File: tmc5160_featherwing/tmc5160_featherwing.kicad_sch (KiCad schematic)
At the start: 3 parts, among them U1 TMC5160A-TA, U2 BUK7D36-60EX, U3 BUK7D36-60EX

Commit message: Add sheets
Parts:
- removed U1: TMC5160A-TA, Package_QFP:TQFP-48-1EP_7x7mm_P0.5mm_EP5x5mm_ThermalVias, symbol Driver_Motor:TMC5160A-TA
- removed U2, U3: BUK7D36-60EX, Janelia:BUK7D3660EX_NEX, symbol Janelia:BUK7D36-60EX
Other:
- added sheet assembly (assembly.kicad_sch)
- added sheet driver_controller (driver_controller.kicad_sch)
- added sheet power (power.kicad_sch)
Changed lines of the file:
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@@
   (title_block
     (title "tmc5160_featherwing")
-    (date "2024-03-21")
+    (date "2024-03-22")
     (rev "1.0")
     (company "Howard Hughes Medical Institute")
   )
-  (symbol (lib_id "Driver_Motor:TMC5160A-TA") (at 49.53 109.22 0) (unit 1)
-    (in_bom yes) (on_board yes) (dnp no) (fields_autoplaced)
-    (property "Reference" "U1" (at 54.2641 147.32 0)
-      (effects (font (size 1.27 1.27)) (justify left))
+  (wire (pts (xy 57.15 38.1) (xy 59.69 38.1))
+    (stroke (width 0) (type default))
+  )
+  (label "GND" (at 57.15 38.1 180) (fields_autoplaced)
+    (effects (font (size 1.27 1.27)) (justify right bottom))
+  )
+  (sheet (at 59.69 60.96) (size 13.97 3.81) (fields_autoplaced)
+    (stroke (width 0.1524) (type solid))
+    (fill (color 0 0 0 0.0000))
+    (property "Sheetname" "driver_controller" (at 59.69 60.2484 0)
+      (effects (font (size 1.27 1.27)) (justify left bottom))
     )
-    (property "Value" "TMC5160A-TA" (at 54.2641 149.86 0)
-      (effects (font (size 1.27 1.27)) (justify left))
+    (property "Sheetfile" "driver_controller.kicad_sch" (at 59.69 65.3546 0)
+      (effects (font (size 1.27 1.27)) (justify left top))
     )
-    (property "Footprint" "Package_QFP:TQFP-48-1EP_7x7mm_P0.5mm_EP5x5mm_ThermalVias" (at 49.53 160.02 0)
-      (effects (font (size 1.27 1.27)) hide)
-    )
-    (property "Datasheet" "https://www.trinamic.com/fileadmin/assets/Products/ICs_Documents/TMC5160A_Datasheet_Rev1.14.pdf" (at 49.53 99.06 0)
-      (effects (font (size 1.27 1.27)) hide)
-    )
-    (pin "20")
-    (pin "3")
-    (pin "37")
-    (pin "38")
-    (pin "8")
-    (pin "47")
-    (pin "49")
-    (pin "21")
-    (pin "33")
-    (pin "35")
-    (pin "9")
-    (pin "5")
-    (pin "14")
-    (pin "11")
-    (pin "15")
-    (pin "6")
-    (pin "18")
-    (pin "41")
-    (pin "43")
-    (pin "32")
-    (pin "26")
-    (pin "48")
-    (pin "39")
-    (pin "17")
-    (pin "7")
-    (pin "30")
-    (pin "29")
-    (pin "34")
-    (pin "46")
-    (pin "24")
-    (pin "31")
-    (pin "25")
-    (pin "19")
-    (pin "2")
-    (pin "4")
-    (pin "28")
-    (pin "16")
-    (pin "23")
-    (pin "36")
-    (pin "10")
-    (pin "40")
-    (pin "22")
-    (pin "27")
-    (pin "44")
-    (pin "13")
-    (pin "12")
-    (pin "1")
-    (pin "45")
-    (pin "42")
     (instances
       (project "tmc5160_featherwing"
-        (path "/df2b2e89-e055-4140-95de-f1df723db034"
-          (reference "U1") (unit 1)
-        )
+        (path "/df2b2e89-e055-4140-95de-f1df723db034" (page "4"))
       )
     )
   )
-  (symbol (lib_id "Janelia:BUK7D36-60EX") (at 180.34 53.34 0) (unit 1)
-    (in_bom yes) (on_board yes) (dnp no) (fields_autoplaced)
-    (property "Reference" "U3" (at 172.72 60.96 0) (do_not_autoplace)
-      (effects (font (size 1.524 1.524)))
+  (sheet (at 59.69 35.56) (size 12.7 5.08) (fields_autoplaced)
+    (stroke (width 0.1524) (type solid))
+    (fill (color 0 0 0 0.0000))
+    (property "Sheetname" "assembly" (at 59.69 34.8484 0)
+      (effects (font (size 1.27 1.27)) (justify left bottom))
     )
-    (property "Value" "BUK7D36-60EX" (at 189.23 53.34 90) (do_not_autoplace)
-      (effects (font (size 1.524 1.524)))
+    (property "Sheetfile" "assembly.kicad_sch" (at 59.69 41.2246 0)
+      (effects (font (size 1.27 1.27)) (justify left top))
     )
-    (property "Footprint" "Janelia:BUK7D3660EX_NEX" (at 180.34 22.86 0)
-      (effects (font (size 1.27 1.27) italic) hide)
+    (pin "GND" passive (at 59.69 38.1 180)
+      (effects (font (size 1.27 1.27)) (justify left))
     )
-    (property "Datasheet" "BUK7D36-60EX" (at 180.34 27.94 0)
-      (effects (font (size 1.27 1.27) italic) hide)
-    )
-    (property "Description" "MOSFET N-CH 60V 5.5A/14A" (at 180.34 30.48 0)
-      (effects (font (size 1.27 1.27)) hide)
-    )
-    (property "Package" "6DFN" (at 180.34 15.24 0)
-      (effects (font (size 1.27 1.27)) hide)
-    )
-    (property "Manufacturer" "Nexperia USA Inc." (at 180.34 20.32 0)
-      (effects (font (size 1.27 1.27)) hide)
-    )
-    (property "Manufacturer Part Number" "BUK7D36-60EX" (at 180.34 12.7 0)
-      (effects (font (size 1.27 1.27)) hide)
-    )
-    (property "Vendor" "Digi-Key" (at 180.34 17.78 0)
-      (effects (font (size 1.27 1.27)) hide)
-    )
-    (property "Vendor Part Number" "1727-BUK7D36-60EXCT-ND" (at 180.34 25.4 0)
-      (effects (font (size 1.27 1.27)) hide)
-    )
-    (pin "4")
-    (pin "5")
-    (pin "6")
-    (pin "8")
-    (pin "3")
-    (pin "2")
-    (pin "1")
-    (pin "7")
     (instances
       (project "tmc5160_featherwing"
-        (path "/df2b2e89-e055-4140-95de-f1df723db034"
-          (reference "U3") (unit 1)
-        )
+        (path "/df2b2e89-e055-4140-95de-f1df723db034" (page "2"))
       )
     )
   )
-  (symbol (lib_id "Janelia:BUK7D36-60EX") (at 135.89 53.34 0) (unit 1)
-    (in_bom yes) (on_board yes) (dnp no) (fields_autoplaced)
-    (property "Reference" "U2" (at 128.27 60.96 0) (do_not_autoplace)
-      (effects (font (size 1.524 1.524)))
+  (sheet (at 59.69 49.53) (size 12.7 3.81) (fields_autoplaced)
+    (stroke (width 0.1524) (type solid))
+    (fill (color 0 0 0 0.0000))
+    (property "Sheetname" "power" (at 59.69 48.8184 0)
+      (effects (font (size 1.27 1.27)) (justify left bottom))
     )
-    (property "Value" "BUK7D36-60EX" (at 144.78 53.34 90) (do_not_autoplace)
-      (effects (font (size 1.524 1.524)))
+    (property "Sheetfile" "power.kicad_sch" (at 59.69 53.9246 0)
+      (effects (font (size 1.27 1.27)) (justify left top))
     )
-    (property "Footprint" "Janelia:BUK7D3660EX_NEX" (at 135.89 22.86 0)
-      (effects (font (size 1.27 1.27) italic) hide)
-    )
-    (property "Datasheet" "BUK7D36-60EX" (at 135.89 27.94 0)
-      (effects (font (size 1.27 1.27) italic) hide)
-    )
-    (property "Description" "MOSFET N-CH 60V 5.5A/14A" (at 135.89 30.48 0)
-      (effects (font (size 1.27 1.27)) hide)
-    )
-    (property "Package" "6DFN" (at 135.89 15.24 0)
-      (effects (font (size 1.27 1.27)) hide)
-    )
-    (property "Manufacturer" "Nexperia USA Inc." (at 135.89 20.32 0)
-      (effects (font (size 1.27 1.27)) hide)
-    )
-    (property "Manufacturer Part Number" "BUK7D36-60EX" (at 135.89 12.7 0)
-      (effects (font (size 1.27 1.27)) hide)
-    )
-    (property "Vendor" "Digi-Key" (at 135.89 17.78 0)
-      (effects (font (size 1.27 1.27)) hide)
-    )
-    (property "Vendor Part Number" "1727-BUK7D36-60EXCT-ND" (at 135.89 25.4 0)
-      (effects (font (size 1.27 1.27)) hide)
-    )
-    (pin "2")
-    (pin "7")
-    (pin "6")
-    (pin "5")
-    (pin "4")
-    (pin "3")
-    (pin "1")
-    (pin "8")
     (instances
       (project "tmc5160_featherwing"
-        (path "/df2b2e89-e055-4140-95de-f1df723db034"
-          (reference "U2") (unit 1)
-        )
+        (path "/df2b2e89-e055-4140-95de-f1df723db034" (page "3"))
       )
     )

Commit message: Add connectors
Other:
- added sheet featherwing (featherwing.kicad_sch)
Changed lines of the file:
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@@
   (title_block
     (title "tmc5160_featherwing")
-    (date "2024-03-22")
+    (date "2024-03-25")
     (rev "1.0")
     (company "Howard Hughes Medical Institute")
@@
     (effects (font (size 1.27 1.27)) (justify right bottom))
   )
-  (sheet (at 59.69 60.96) (size 13.97 3.81) (fields_autoplaced)
+  (sheet (at 59.69 72.39) (size 13.97 3.81) (fields_autoplaced)
     (stroke (width 0.1524) (type solid))
     (fill (color 0 0 0 0.0000))
-    (property "Sheetname" "driver_controller" (at 59.69 60.2484 0)
+    (property "Sheetname" "driver_controller" (at 59.69 71.6784 0)
       (effects (font (size 1.27 1.27)) (justify left bottom))
     )
-    (property "Sheetfile" "driver_controller.kicad_sch" (at 59.69 65.3546 0)
+    (property "Sheetfile" "driver_controller.kicad_sch" (at 59.69 76.7846 0)
       (effects (font (size 1.27 1.27)) (justify left top))
     )
@@
     )
   )
-  (sheet (at 59.69 49.53) (size 12.7 3.81) (fields_autoplaced)
+  (sheet (at 59.69 48.26) (size 12.7 3.81) (fields_autoplaced)
     (stroke (width 0.1524) (type solid))
     (fill (color 0 0 0 0.0000))
-    (property "Sheetname" "power" (at 59.69 48.8184 0)
+    (property "Sheetname" "featherwing" (at 59.69 47.5484 0)
       (effects (font (size 1.27 1.27)) (justify left bottom))
     )
-    (property "Sheetfile" "power.kicad_sch" (at 59.69 53.9246 0)
+    (property "Sheetfile" "featherwing.kicad_sch" (at 59.69 52.6546 0)
       (effects (font (size 1.27 1.27)) (justify left top))
     )
+    (instances
+      (project "tmc5160_featherwing"
+        (path "/df2b2e89-e055-4140-95de-f1df723db034" (page "13"))
+      )
+    )
+  )
+  (sheet (at 59.69 60.96) (size 12.7 3.81) (fields_autoplaced)
+    (stroke (width 0.1524) (type solid))
+    (fill (color 0 0 0 0.0000))
+    (property "Sheetname" "power" (at 59.69 60.2484 0)
+      (effects (font (size 1.27 1.27)) (justify left bottom))
+    )
+    (property "Sheetfile" "power.kicad_sch" (at 59.69 65.3546 0)
+      (effects (font (size 1.27 1.27)) (justify left top))
+    )

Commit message: Add to power sheet
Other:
- sheet power ports: added ENABLE, GND, VIO, VM; removed none
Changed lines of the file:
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@@
   (title_block
     (title "tmc5160_featherwing")
-    (date "2024-04-04")
+    (date "2024-04-05")
     (rev "1.0")
     (company "Howard Hughes Medical Institute")
   )
-  (wire (pts (xy 57.15 38.1) (xy 59.69 38.1))
+  (wire (pts (xy 77.47 48.26) (xy 74.93 48.26))
     (stroke (width 0) (type default))
   )
-  (label "GND" (at 57.15 38.1 180) (fields_autoplaced)
+  (wire (pts (xy 55.88 38.1) (xy 58.42 38.1))
+    (stroke (width 0) (type default))
+  )
+  (wire (pts (xy 77.47 53.34) (xy 74.93 53.34))
+    (stroke (width 0) (type default))
+  )
+  (wire (pts (xy 77.47 50.8) (xy 74.93 50.8))
+    (stroke (width 0) (type default))
+  )
+  (label "GND" (at 77.47 53.34 0) (fields_autoplaced)
+    (effects (font (size 1.27 1.27)) (justify left bottom))
+  )
+  (label "VIO" (at 77.47 50.8 0) (fields_autoplaced)
+    (effects (font (size 1.27 1.27)) (justify left bottom))
+  )
+  (label "GND" (at 55.88 38.1 180) (fields_autoplaced)
     (effects (font (size 1.27 1.27)) (justify right bottom))
   )
-  (sheet (at 59.69 72.39) (size 13.97 3.81) (fields_autoplaced)
+  (label "VM" (at 77.47 48.26 0) (fields_autoplaced)
+    (effects (font (size 1.27 1.27)) (justify left bottom))
+  )
+  (sheet (at 58.42 78.74) (size 13.97 3.81) (fields_autoplaced)
     (stroke (width 0.1524) (type solid))
     (fill (color 0 0 0 0.0000))
-    (property "Sheetname" "driver_controller" (at 59.69 71.6784 0)
+    (property "Sheetname" "driver_controller" (at 58.42 78.0284 0)
       (effects (font (size 1.27 1.27)) (justify left bottom))
     )
-    (property "Sheetfile" "driver_controller.kicad_sch" (at 59.69 76.7846 0)
+    (property "Sheetfile" "driver_controller.kicad_sch" (at 58.42 83.1346 0)
       (effects (font (size 1.27 1.27)) (justify left top))
     )
@@
     )
   )
-  (sheet (at 59.69 35.56) (size 12.7 5.08) (fields_autoplaced)
+  (sheet (at 58.42 35.56) (size 12.7 5.08) (fields_autoplaced)
     (stroke (width 0.1524) (type solid))
     (fill (color 0 0 0 0.0000))
-    (property "Sheetname" "assembly" (at 59.69 34.8484 0)
+    (property "Sheetname" "assembly" (at 58.42 34.8484 0)
       (effects (font (size 1.27 1.27)) (justify left bottom))
     )
-    (property "Sheetfile" "assembly.kicad_sch" (at 59.69 41.2246 0)
+    (property "Sheetfile" "assembly.kicad_sch" (at 58.42 41.2246 0)
       (effects (font (size 1.27 1.27)) (justify left top))
     )
-    (pin "GND" passive (at 59.69 38.1 180)
+    (pin "GND" passive (at 58.42 38.1 180)
       (effects (font (size 1.27 1.27)) (justify left))
     )
@@
     )
   )
-  (sheet (at 59.69 48.26) (size 12.7 3.81) (fields_autoplaced)
+  (sheet (at 58.42 63.5) (size 12.7 3.81) (fields_autoplaced)
     (stroke (width 0.1524) (type solid))
     (fill (color 0 0 0 0.0000))
-    (property "Sheetname" "featherwing" (at 59.69 47.5484 0)
+    (property "Sheetname" "featherwing" (at 58.42 62.7884 0)
       (effects (font (size 1.27 1.27)) (justify left bottom))
     )
-    (property "Sheetfile" "featherwing.kicad_sch" (at 59.69 52.6546 0)
+    (property "Sheetfile" "featherwing.kicad_sch" (at 58.42 67.8946 0)
       (effects (font (size 1.27 1.27)) (justify left top))
     )
@@
     )
   )
-  (sheet (at 59.69 60.96) (size 12.7 3.81) (fields_autoplaced)
+  (sheet (at 58.42 45.72) (size 16.51 10.16) (fields_autoplaced)
     (stroke (width 0.1524) (type solid))
     (fill (color 0 0 0 0.0000))
-    (property "Sheetname" "power" (at 59.69 60.2484 0)
+    (property "Sheetname" "power" (at 58.42 45.0084 0)
       (effects (font (size 1.27 1.27)) (justify left bottom))
     )
-    (property "Sheetfile" "power.kicad_sch" (at 59.69 65.3546 0)
+    (property "Sheetfile" "power.kicad_sch" (at 58.42 56.4646 0)
       (effects (font (size 1.27 1.27)) (justify left top))
     )
+    (pin "GND" passive (at 74.93 53.34 0)
+      (effects (font (size 1.27 1.27)) (justify right))
+    )
+    (pin "VM" passive (at 74.93 48.26 0)
+      (effects (font (size 1.27 1.27)) (justify right))
+    )
+    (pin "VIO" passive (at 74.93 50.8 0)
+      (effects (font (size 1.27 1.27)) (justify right))
+    )
+    (pin "ENABLE" input (at 58.42 50.8 180)
+      (effects (font (size 1.27 1.27)) (justify left))
+    )
     (instances

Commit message: Add parts
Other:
- sheet driver_controller ports: added GND, VIO, VM; removed none
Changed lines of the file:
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@@
   (title_block
     (title "tmc5160_featherwing")
-    (date "2024-04-05")
+    (date "2024-04-10")
     (rev "1.0")
     (company "Howard Hughes Medical Institute")
+  )
+  (wire (pts (xy 55.88 83.82) (xy 58.42 83.82))
+    (stroke (width 0) (type default))
   )
   (wire (pts (xy 77.47 48.26) (xy 74.93 48.26))
@@
   )
   (wire (pts (xy 55.88 38.1) (xy 58.42 38.1))
+    (stroke (width 0) (type default))
+  )
+  (wire (pts (xy 55.88 81.28) (xy 58.42 81.28))
+    (stroke (width 0) (type default))
+  )
+  (wire (pts (xy 55.88 86.36) (xy 58.42 86.36))
     (stroke (width 0) (type default))
   )
@@
     (effects (font (size 1.27 1.27)) (justify left bottom))
   )
+  (label "VIO" (at 55.88 83.82 180) (fields_autoplaced)
+    (effects (font (size 1.27 1.27)) (justify right bottom))
+  )
+  (label "VM" (at 55.88 81.28 180) (fields_autoplaced)
+    (effects (font (size 1.27 1.27)) (justify right bottom))
+  )
   (label "GND" (at 55.88 38.1 180) (fields_autoplaced)
+    (effects (font (size 1.27 1.27)) (justify right bottom))
+  )
+  (label "GND" (at 55.88 86.36 180) (fields_autoplaced)
     (effects (font (size 1.27 1.27)) (justify right bottom))
   )
@@
     (effects (font (size 1.27 1.27)) (justify left bottom))
   )
-  (sheet (at 58.42 78.74) (size 13.97 3.81) (fields_autoplaced)
+  (sheet (at 58.42 78.74) (size 16.51 12.7) (fields_autoplaced)
     (stroke (width 0.1524) (type solid))
     (fill (color 0 0 0 0.0000))
@@
       (effects (font (size 1.27 1.27)) (justify left bottom))
     )
-    (property "Sheetfile" "driver_controller.kicad_sch" (at 58.42 83.1346 0)
+    (property "Sheetfile" "driver_controller.kicad_sch" (at 58.42 92.0246 0)
       (effects (font (size 1.27 1.27)) (justify left top))
     )
+    (pin "VM" passive (at 58.42 81.28 180)
+      (effects (font (size 1.27 1.27)) (justify left))
+    )
+    (pin "VIO" passive (at 58.42 83.82 180)
+      (effects (font (size 1.27 1.27)) (justify left))
+    )
+    (pin "GND" passive (at 58.42 86.36 180)
+      (effects (font (size 1.27 1.27)) (justify left))
+    )
     (instances

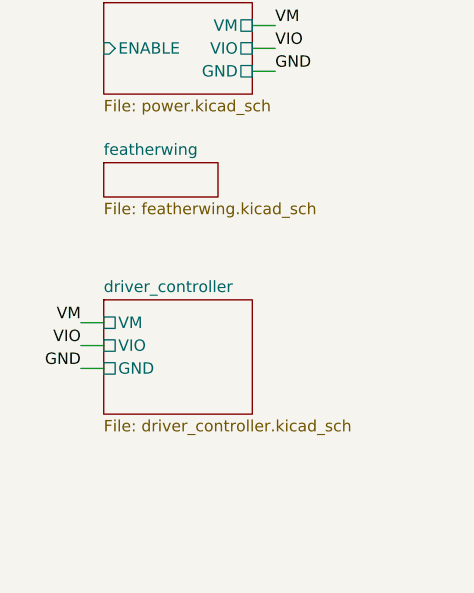
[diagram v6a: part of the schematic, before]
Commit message: Add capacitors and resistors
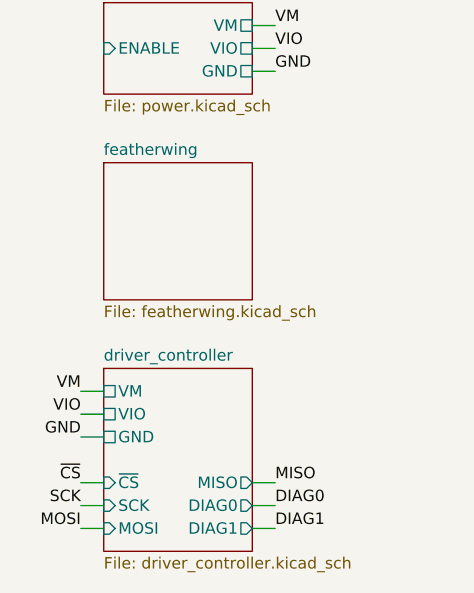
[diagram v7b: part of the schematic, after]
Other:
- sheet driver_controller ports: added DIAG0, DIAG1, MISO, MOSI, SCK, ~{CS}; removed none
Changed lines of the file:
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@@
   (title_block
     (title "tmc5160_featherwing")
-    (date "2024-04-11")
+    (date "2024-04-12")
     (rev "1.0")
     (company "Howard Hughes Medical Institute")
   )
-  (wire (pts (xy 55.88 83.82) (xy 58.42 83.82))
+  (wire (pts (xy 58.42 101.6) (xy 55.88 101.6))
+    (stroke (width 0) (type default))
+  )
+  (wire (pts (xy 55.88 91.44) (xy 58.42 91.44))
+    (stroke (width 0) (type default))
+  )
+  (wire (pts (xy 58.42 104.14) (xy 55.88 104.14))
     (stroke (width 0) (type default))
   )
@@
     (stroke (width 0) (type default))
   )
+  (wire (pts (xy 58.42 99.06) (xy 55.88 99.06))
+    (stroke (width 0) (type default))
+  )
+  (wire (pts (xy 74.93 104.14) (xy 77.47 104.14))
+    (stroke (width 0) (type default))
+  )
   (wire (pts (xy 55.88 38.1) (xy 58.42 38.1))
     (stroke (width 0) (type default))
   )
-  (wire (pts (xy 55.88 81.28) (xy 58.42 81.28))
+  (wire (pts (xy 55.88 88.9) (xy 58.42 88.9))
     (stroke (width 0) (type default))
   )
-  (wire (pts (xy 55.88 86.36) (xy 58.42 86.36))
+  (wire (pts (xy 74.93 101.6) (xy 77.47 101.6))
+    (stroke (width 0) (type default))
+  )
+  (wire (pts (xy 74.93 99.06) (xy 77.47 99.06))
+    (stroke (width 0) (type default))
+  )
+  (wire (pts (xy 55.88 93.98) (xy 58.42 93.98))
     (stroke (width 0) (type default))
   )
@@
     (effects (font (size 1.27 1.27)) (justify left bottom))
   )
+  (label "DIAG1" (at 77.47 104.14 0) (fields_autoplaced)
+    (effects (font (size 1.27 1.27)) (justify left bottom))
+  )
   (label "VIO" (at 77.47 50.8 0) (fields_autoplaced)
     (effects (font (size 1.27 1.27)) (justify left bottom))
   )
-  (label "VIO" (at 55.88 83.82 180) (fields_autoplaced)
+  (label "MOSI" (at 55.88 104.14 180) (fields_autoplaced)
     (effects (font (size 1.27 1.27)) (justify right bottom))
   )
-  (label "VM" (at 55.88 81.28 180) (fields_autoplaced)
+  (label "VIO" (at 55.88 91.44 180) (fields_autoplaced)
     (effects (font (size 1.27 1.27)) (justify right bottom))
+  )
+  (label "VM" (at 55.88 88.9 180) (fields_autoplaced)
+    (effects (font (size 1.27 1.27)) (justify right bottom))
+  )
+  (label "DIAG0" (at 77.47 101.6 0) (fields_autoplaced)
+    (effects (font (size 1.27 1.27)) (justify left bottom))
   )
   (label "GND" (at 55.88 38.1 180) (fields_autoplaced)
     (effects (font (size 1.27 1.27)) (justify right bottom))
   )
-  (label "GND" (at 55.88 86.36 180) (fields_autoplaced)
+  (label "GND" (at 55.88 93.98 180) (fields_autoplaced)
+    (effects (font (size 1.27 1.27)) (justify right bottom))
+  )
+  (label "MISO" (at 77.47 99.06 0) (fields_autoplaced)
+    (effects (font (size 1.27 1.27)) (justify left bottom))
+  )
+  (label "SCK" (at 55.88 101.6 180) (fields_autoplaced)
+    (effects (font (size 1.27 1.27)) (justify right bottom))
+  )
+  (label "~{CS}" (at 55.88 99.06 180) (fields_autoplaced)
     (effects (font (size 1.27 1.27)) (justify right bottom))
   )
@@
     (effects (font (size 1.27 1.27)) (justify left bottom))
   )
-  (sheet (at 58.42 78.74) (size 16.51 12.7) (fields_autoplaced)
+  (sheet (at 58.42 86.36) (size 16.51 20.32) (fields_autoplaced)
     (stroke (width 0.1524) (type solid))
     (fill (color 0 0 0 0.0000))
-    (property "Sheetname" "driver_controller" (at 58.42 78.0284 0)
+    (property "Sheetname" "driver_controller" (at 58.42 85.6484 0)
       (effects (font (size 1.27 1.27)) (justify left bottom))
     )
-    (property "Sheetfile" "driver_controller.kicad_sch" (at 58.42 92.0246 0)
+    (property "Sheetfile" "driver_controller.kicad_sch" (at 58.42 107.2646 0)
       (effects (font (size 1.27 1.27)) (justify left top))
     )
-    (pin "VM" passive (at 58.42 81.28 180)
+    (pin "VM" passive (at 58.42 88.9 180)
       (effects (font (size 1.27 1.27)) (justify left))
     )
-    (pin "VIO" passive (at 58.42 83.82 180)
+    (pin "VIO" passive (at 58.42 91.44 180)
       (effects (font (size 1.27 1.27)) (justify left))
     )
-    (pin "GND" passive (at 58.42 86.36 180)
+    (pin "GND" passive (at 58.42 93.98 180)
+      (effects (font (size 1.27 1.27)) (justify left))
+    )
+    (pin "~{CS}" input (at 58.42 99.06 180)
+      (effects (font (size 1.27 1.27)) (justify left))
+    )
+    (pin "SCK" input (at 58.42 101.6 180)
+      (effects (font (size 1.27 1.27)) (justify left))
+    )
+    (pin "DIAG0" output (at 74.93 101.6 0)
+      (effects (font (size 1.27 1.27)) (justify right))
+    )
+    (pin "DIAG1" output (at 74.93 104.14 0)
+      (effects (font (size 1.27 1.27)) (justify right))
+    )
+    (pin "MISO" output (at 74.93 99.06 0)
+      (effects (font (size 1.27 1.27)) (justify right))
+    )
+    (pin "MOSI" input (at 58.42 104.14 180)
       (effects (font (size 1.27 1.27)) (justify left))
     )
@@
     )
   )
-  (sheet (at 58.42 63.5) (size 12.7 3.81) (fields_autoplaced)
+  (sheet (at 58.42 63.5) (size 16.51 15.24) (fields_autoplaced)
     (stroke (width 0.1524) (type solid))
     (fill (color 0 0 0 0.0000))
@@
       (effects (font (size 1.27 1.27)) (justify left bottom))
     )
-    (property "Sheetfile" "featherwing.kicad_sch" (at 58.42 67.8946 0)
+    (property "Sheetfile" "featherwing.kicad_sch" (at 58.42 79.3246 0)
       (effects (font (size 1.27 1.27)) (justify left top))
     )
